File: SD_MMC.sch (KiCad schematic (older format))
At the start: 14 parts, among them J3 Micro_SD_Card, U1 IMX8MM, U5 SDINBDG4-8G

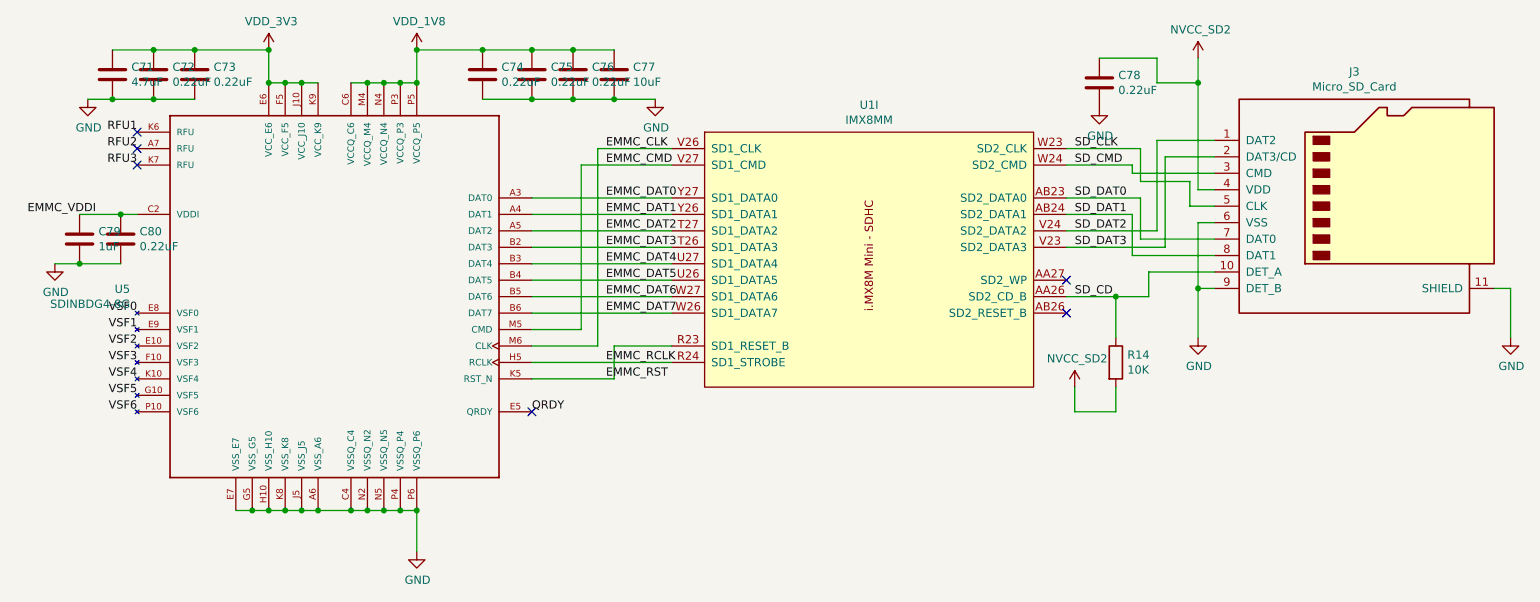
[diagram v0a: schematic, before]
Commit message: Re-annotate schematics, add dnp field, and silkscreen cleanup
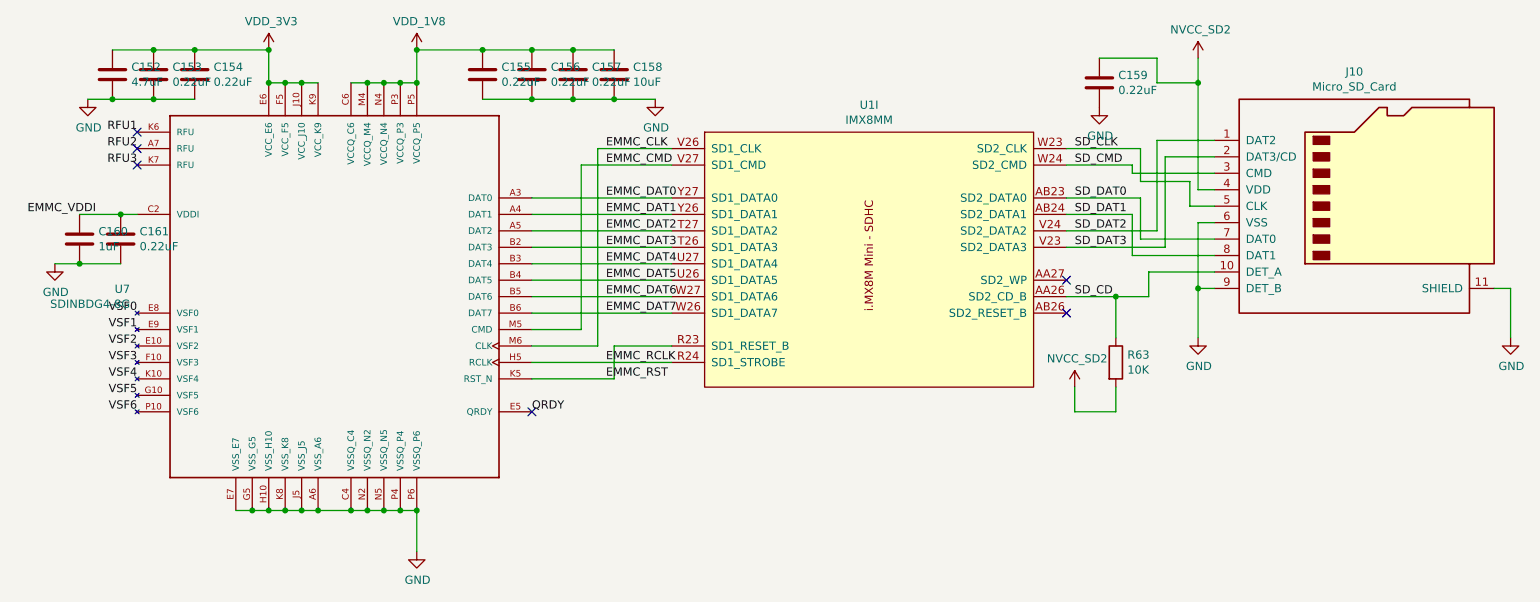
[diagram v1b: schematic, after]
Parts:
- renumbered C71 to C152, C72 to C153, C73 to C154, C74 to C155, C75 to C156, C76 to C157, C77 to C158, C78 to C159, C79 to C160, C80 to C161, J3 to J10, R14 to R63, U5 to U7
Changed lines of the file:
@@
 	9400 5500 9700 5500
 $Comp
-L power:GND #PWR0138
+L power:GND #PWR0184
 U 1 1 5D1EE7E1
 P 5450 7050
-F 0 "#PWR0138" H 5450 6800 50  0001 C CNN
+F 0 "#PWR0184" H 5450 6800 50  0001 C CNN
 F 1 "GND" H 5455 6877 50  0000 C CNN
 F 2 "" H 5450 7050 50  0001 C CNN
@@
 	5450 7050 5450 6800
 $Comp
-L power:GND #PWR0139
+L power:GND #PWR0180
 U 1 1 5D1F1F8F
 P 3250 5300
-F 0 "#PWR0139" H 3250 5050 50  0001 C CNN
+F 0 "#PWR0180" H 3250 5050 50  0001 C CNN
 F 1 "GND" H 3255 5127 50  0000 C CNN
 F 2 "" H 3250 5300 50  0001 C CNN
@@
 	4550 4000 4550 4200
 $Comp
-L mxenc:VDD_1V8 #PWR0140
+L mxenc:VDD_1V8 #PWR0175
 U 1 1 5D1FA598
 P 5450 4000
-F 0 "#PWR0140" H 5450 3850 50  0001 C CNN
+F 0 "#PWR0175" H 5450 3850 50  0001 C CNN
 F 1 "VDD_1V8" H 5465 4173 50  0000 C CNN
 F 2 "" H 5450 4000 50  0001 C CNN
@@
 	5450 4000 5450 4200
 $Comp
-L mxenc:VDD_3V3 #PWR0141
+L mxenc:VDD_3V3 #PWR0174
 U 1 1 5D203F1C
 P 4550 4000
-F 0 "#PWR0141" H 4550 3850 50  0001 C CNN
+F 0 "#PWR0174" H 4550 3850 50  0001 C CNN
 F 1 "VDD_3V3" H 4565 4173 50  0000 C CNN
 F 2 "" H 4550 4000 50  0001 C CNN
@@
 	10200 4850 10300 4850
 $Comp
-L power:GND #PWR0143
+L power:GND #PWR0181
 U 1 1 5D208059
 P 10200 5750
-F 0 "#PWR0143" H 10200 5500 50  0001 C CNN
+F 0 "#PWR0181" H 10200 5500 50  0001 C CNN
 F 1 "GND" H 10205 5577 50  0000 C CNN
 F 2 "" H 10200 5750 50  0001 C CNN
@@
 	10300 5050 10200 5050
 $Comp
-L Device:R R14
+L Device:R R63
 U 1 1 5D20EA8C
 P 9700 5900
-F 0 "R14" H 9770 5946 50  0000 L CNN
+F 0 "R63" H 9770 5946 50  0000 L CNN
 F 1 "10K" H 9770 5855 50  0000 L CNN
 F 2 "Resistor_SMD:R_0402_1005Metric" V 9630 5900 50  0001 C CNN
@@
 	9700 6200 9700 6050
 $Comp
-L Device:C C78
+L Device:C C159
 U 1 1 5D22524F
 P 9600 4200
-F 0 "C78" H 9715 4246 50  0000 L CNN
+F 0 "C159" H 9715 4246 50  0000 L CNN
 F 1 "0.22uF" H 9715 4155 50  0000 L CNN
 F 2 "Capacitor_SMD:C_0402_1005Metric" H 9638 4050 50  0001 C CNN
@@
 	10200 4200 10200 4850
 $Comp
-L power:GND #PWR0145
+L power:GND #PWR0179
 U 1 1 5D227DD8
 P 9600 4350
-F 0 "#PWR0145" H 9600 4100 50  0001 C CNN
+F 0 "#PWR0179" H 9600 4100 50  0001 C CNN
 F 1 "GND" H 9605 4177 50  0000 C CNN
 F 2 "" H 9600 4350 50  0001 C CNN
@@
 	9600 4050 9950 4050
 $Comp
-L Device:C C74
+L Device:C C155
 U 1 1 5D22B9CE
 P 5850 4150
-F 0 "C74" H 5965 4196 50  0000 L CNN
+F 0 "C155" H 5965 4196 50  0000 L CNN
 F 1 "0.22uF" H 5965 4105 50  0000 L CNN
 F 2 "Capacitor_SMD:C_0201_0603Metric" H 5888 4000 50  0001 C CNN
@@
 	6150 4000 5850 4000
 $Comp
-L Device:C C75
+L Device:C C156
 U 1 1 5D22C3F2
 P 6150 4150
-F 0 "C75" H 6265 4196 50  0000 L CNN
+F 0 "C156" H 6265 4196 50  0000 L CNN
 F 1 "0.22uF" H 6265 4105 50  0000 L CNN
 F 2 "Capacitor_SMD:C_0201_0603Metric" H 6188 4000 50  0001 C CNN
@@
 	6400 4300 6150 4300
 $Comp
-L Device:C C76
+L Device:C C157
 U 1 1 5D22CACC
 P 6400 4150
-F 0 "C76" H 6515 4196 50  0000 L CNN
+F 0 "C157" H 6515 4196 50  0000 L CNN
 F 1 "0.22uF" H 6515 4105 50  0000 L CNN
 F 2 "Capacitor_SMD:C_0201_0603Metric" H 6438 4000 50  0001 C CNN
@@
 	6650 4300 6400 4300
 $Comp
-L Device:C C77
+L Device:C C158
 U 1 1 5D22CFC3
 P 6650 4150
-F 0 "C77" H 6765 4196 50  0000 L CNN
+F 0 "C158" H 6765 4196 50  0000 L CNN
 F 1 "10uF" H 6765 4105 50  0000 L CNN
 F 2 "Capacitor_SMD:C_0402_1005Metric" H 6688 4000 50  0001 C CNN
@@
 	6900 4300 6650 4300
 $Comp
-L power:GND #PWR0146
+L power:GND #PWR0178
 U 1 1 5D22FD79
 P 6900 4300
-F 0 "#PWR0146" H 6900 4050 50  0001 C CNN
+F 0 "#PWR0178" H 6900 4050 50  0001 C CNN
 F 1 "GND" H 6905 4127 50  0000 C CNN
 F 2 "" H 6900 4300 50  0001 C CNN
@@
 $EndComp
 $Comp
-L Device:C C73
+L Device:C C154
 U 1 1 5D233CD7
 P 4100 4150
-F 0 "C73" H 4215 4196 50  0000 L CNN
+F 0 "C154" H 4215 4196 50  0000 L CNN
 F 1 "0.22uF" H 4215 4105 50  0000 L CNN
 F 2 "Capacitor_SMD:C_0201_0603Metric" H 4138 4000 50  0001 C CNN
@@
 	3850 4000 4100 4000
 $Comp
-L power:GND #PWR0147
+L power:GND #PWR0177
 U 1 1 5D23728B
 P 3450 4300
-F 0 "#PWR0147" H 3450 4050 50  0001 C CNN
+F 0 "#PWR0177" H 3450 4050 50  0001 C CNN
 F 1 "GND" H 3455 4127 50  0000 C CNN
 F 2 "" H 3450 4300 50  0001 C CNN
@@
 $EndComp
 $Comp
-L Device:C C72
+L Device:C C153
 U 1 1 5D23E76A
 P 3850 4150
-F 0 "C72" H 3965 4196 50  0000 L CNN
+F 0 "C153" H 3965 4196 50  0000 L CNN
 F 1 "0.22uF" H 3965 4105 50  0000 L CNN
 F 2 "Capacitor_SMD:C_0201_0603Metric" H 3888 4000 50  0001 C CNN
@@
 Connection ~ 3600 4300
 $Comp
-L Device:C C71
+L Device:C C152
 U 1 1 5D241942
 P 3600 4150
-F 0 "C71" H 3715 4196 50  0000 L CNN
+F 0 "C152" H 3715 4196 50  0000 L CNN
 F 1 "4.7uF" H 3715 4105 50  0000 L CNN
 F 2 "Capacitor_SMD:C_0402_1005Metric" H 3638 4000 50  0001 C CNN
@@
 $EndComp
 $Comp
-L Device:C C80
+L Device:C C161
 U 1 1 5D249BD2
 P 3650 5150
-F 0 "C80" H 3765 5196 50  0000 L CNN
+F 0 "C161" H 3765 5196 50  0000 L CNN
 F 1 "0.22uF" H 3765 5105 50  0000 L CNN
 F 2 "Capacitor_SMD:C_0201_0603Metric" H 3688 5000 50  0001 C CNN
@@
 	3650 5000 3750 5000
 $Comp
-L Device:C C79
+L Device:C C160
 U 1 1 5D24A432
 P 3400 5150
-F 0 "C79" H 3515 5196 50  0000 L CNN
+F 0 "C160" H 3515 5196 50  0000 L CNN
 F 1 "1uF" H 3515 5105 50  0000 L CNN
 F 2 "Capacitor_SMD:C_0402_1005Metric" H 3438 5000 50  0001 C CNN
@@
 	10200 5050 10200 5450
 $Comp
-L Connector:Micro_SD_Card_Det J3
+L Connector:Micro_SD_Card_Det J10
 U 1 1 5D3E77AB
 P 11200 4950
-F 0 "J3" H 11150 5767 50  0000 C CNN
+F 0 "J10" H 11150 5767 50  0000 C CNN
 F 1 "Micro_SD_Card" H 11150 5676 50  0000 C CNN
 F 2 "mxenc:114-00841-68" H 12350 5250 50  0001 C CNN
@@
 NoConn ~ 9400 5400
 $Comp
-L mxenc:NVCC_SD2 #PWR0144
+L mxenc:NVCC_SD2 #PWR0176
 U 1 1 5DC50CF4
 P 10200 4050
-F 0 "#PWR0144" H 10200 3900 50  0001 C CNN
+F 0 "#PWR0176" H 10200 3900 50  0001 C CNN
 F 1 "NVCC_SD2" H 10215 4223 50  0000 C CNN
 F 2 "" H 10200 4050 50  0001 C CNN
@@
 	10200 4050 10200 4200
 $Comp
-L mxenc:NVCC_SD2 #PWR0243
+L mxenc:NVCC_SD2 #PWR0183
 U 1 1 5DC5A2D8
 P 9450 6050
-F 0 "#PWR0243" H 9450 5900 50  0001 C CNN
+F 0 "#PWR0183" H 9450 5900 50  0001 C CNN
 F 1 "NVCC_SD2" H 9465 6223 50  0000 C CNN
 F 2 "" H 9450 6050 50  0001 C CNN
@@
 Connection ~ 4450 6800
 $Comp
-L mxenc:SDINBDG4-8G U5
+L mxenc:SDINBDG4-8G U7
 U 1 1 5D196F4B
 P 4950 5500
-F 0 "U5" H 3707 5546 50  0000 R CNN
+F 0 "U7" H 3707 5546 50  0000 R CNN
 F 1 "SDINBDG4-8G" H 3707 5455 50  0000 R CNN
 F 2 "mxenc:BGA153C50P14X14_1300X1150X80N" H 4950 5500 50  0001 L BNN
@@
 	10200 5450 10200 5750
 $Comp
-L power:GND #PWR0150
+L power:GND #PWR0182
 U 1 1 5E2D7AF8
 P 12100 5750
-F 0 "#PWR0150" H 12100 5500 50  0001 C CNN
+F 0 "#PWR0182" H 12100 5500 50  0001 C CNN
 F 1 "GND" H 12105 5577 50  0000 C CNN
 F 2 "" H 12100 5750 50  0001 C CNN
